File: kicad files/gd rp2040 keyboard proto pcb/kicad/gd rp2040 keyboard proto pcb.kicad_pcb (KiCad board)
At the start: 2 copper layers, 81.3 x 49.5 mm, 46 parts, among them J1 USB Pwr, J10 CTRL1-HDR, J11 CTRL2-HDR, J12 USB_A, J14 GPIO, J15 ADC, J2 Conn_01x02, J3 Power, J4 FTDI Header, J5 CTRL1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

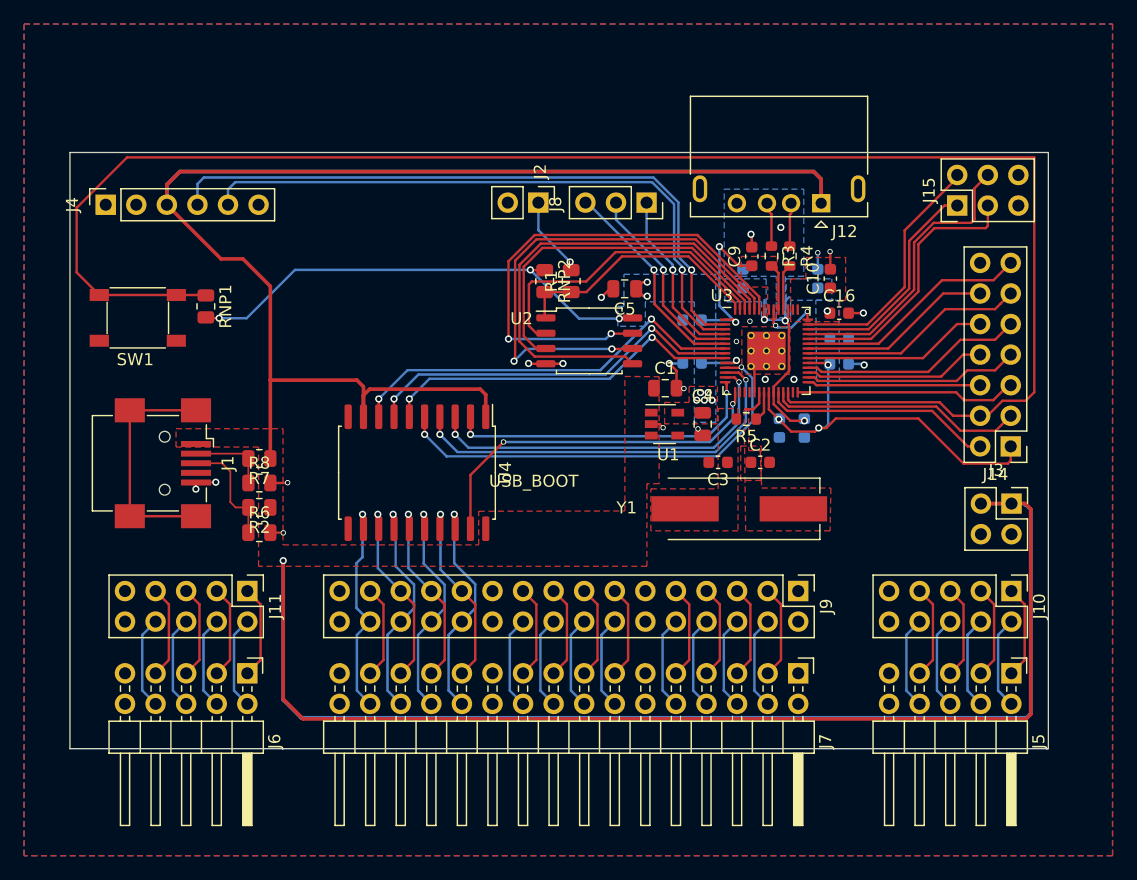
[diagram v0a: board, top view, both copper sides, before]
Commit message: schooched the left edge over to make mini-usb slightly hang over. added some GND vias through the board. re-routed some 3v3 signals for cleaner routes.
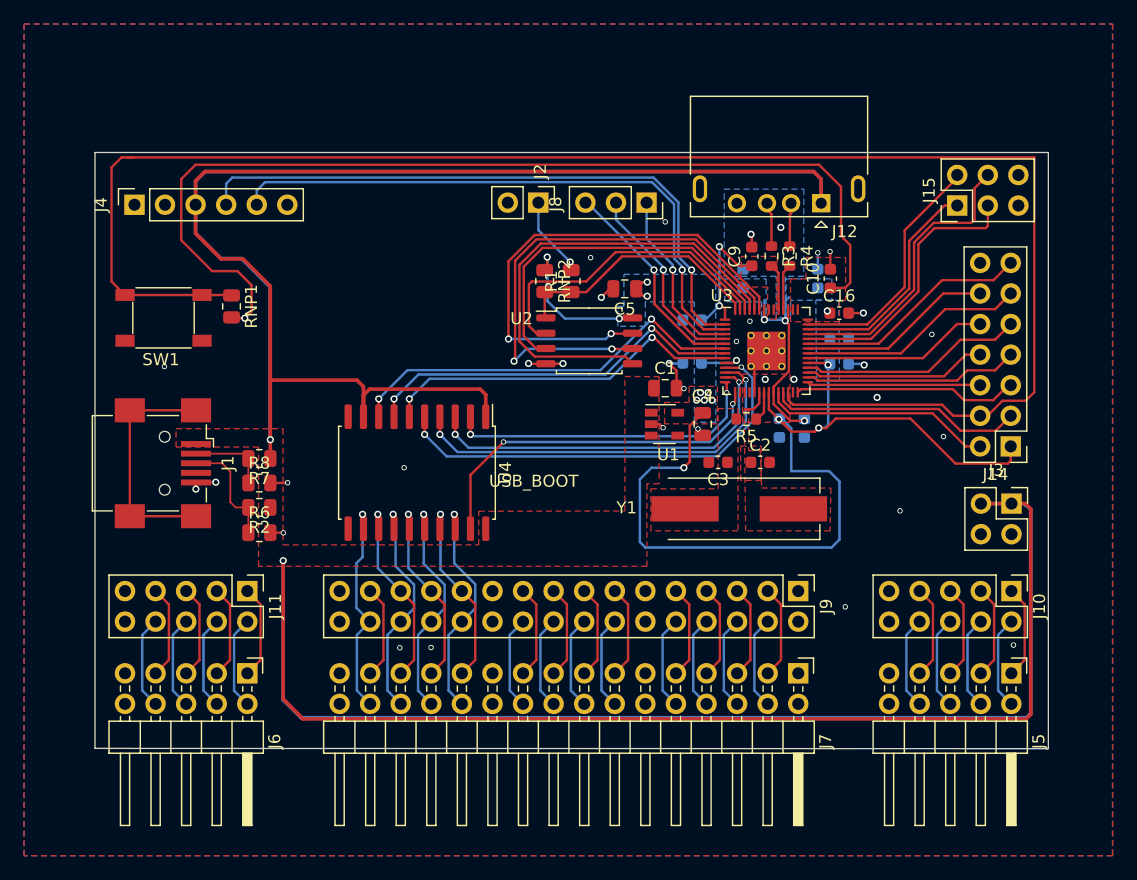
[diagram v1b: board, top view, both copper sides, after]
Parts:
- moved J4 2.39 mm to (67.6, 90.7)
- moved RNP1 2.13 mm to (75.7, 99.1)
- moved SW1 2.13 mm to (70.0, 100.1)
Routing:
- net +3V3: track 99.0 -> 192.0 mm, vias 19 -> 18
- net +5V: track 359.4 -> 377.1 mm, vias 1 -> 2
- net /TX_2040: track 52.6 -> 50.2 mm
- net /RX_2040: track 55.5 -> 53.1 mm
- net /RUN: track 140.1 -> 139.4 mm
- net GND: vias 21 -> 33
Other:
- board size 81.3 x 49.5 mm -> 79.2 x 49.5 mm

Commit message: silk clean up
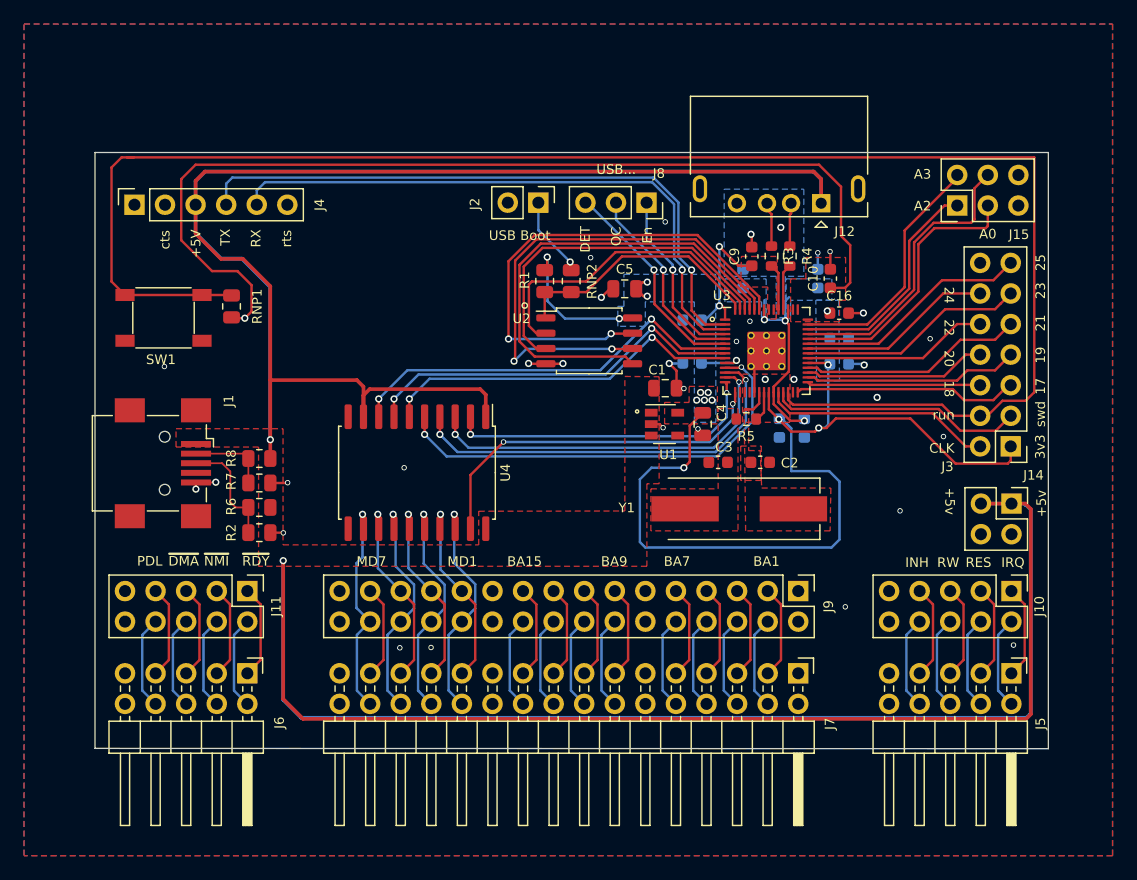
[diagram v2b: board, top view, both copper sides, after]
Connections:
- J1 pad 6: Net-(J1-Pad6) -> GND
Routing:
- net Net-(J1-Pad6): track 19.8 -> 0.00 mm
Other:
- board text added: "+5V"
- board text added: "+5v"
- board text added: "17"
- board text added: "18"
- board text added: "19"
- board text added: "20"
- board text added: "21"
- board text added: "22"
- board text added: "23"
- board text added: "24"
- board text added: "25"
- board text added: "3v3"
- board text added: "A0"
- board text added: "A2"
- board text added: "A3"
- board text added: "BA1"
- board text added: "BA15"
- board text added: "BA7"
- board text added: "BA9"
- board text added: "CLK"
- board text added: "D+"
- board text added: "D-"
- board text added: "DET"
- board text added: "En"
- board text added: "INH"
- board text added: "IRQ"
- board text added: "J10"
- board text added: "J11"
- board text added: "J2"
- board text added: "J5"
- board text added: "J6"
- board text added: "J7"
- board text added: "J8"
- board text added: "J9"
- board text added: "MD1"
- board text added: "MD7"
- board text added: "OC"
- board text added: "PDL"
- board text added: "RES"
- board text added: "RW"
- board text added: "RX"
- board text added: "TX"
- board text added: "USB Boot"
- board text added: "USB..."
- board text added: "cts"
- board text added: "rts"
- board text added: "run"
- board text added: "swd"
- board text added: "~DMA"
- board text added: "~NMI"
- board text added: "~RDY"
- board text removed: "USB_BOOT"

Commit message: rounded corners and added prototype area
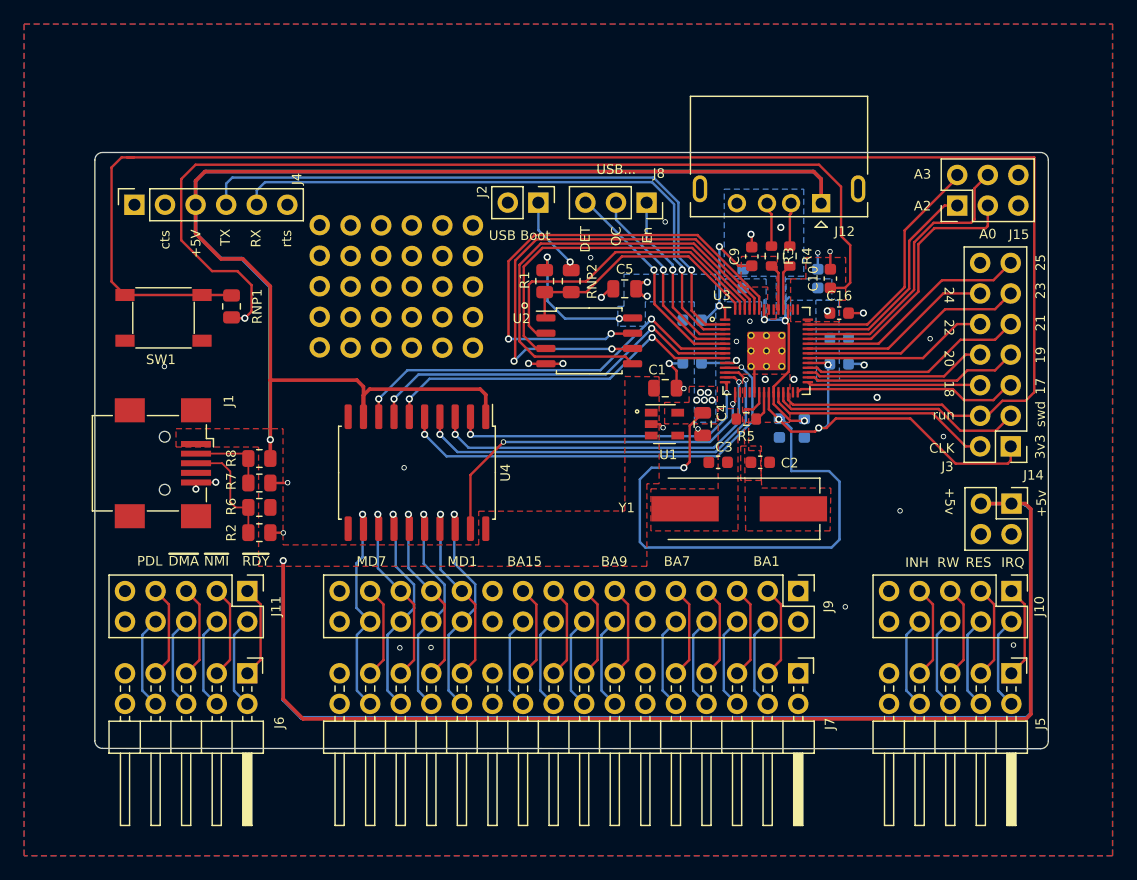
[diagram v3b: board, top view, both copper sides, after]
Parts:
- added J13: Conn_01x04, My Libraries:HoleField_1x05_P2.54mm, F.Cu at (83.0, 92.4)
- added J13: Conn_01x04, My Libraries:HoleField_1x05_P2.54mm, F.Cu at (85.5, 92.4)
- added J13: Conn_01x04, My Libraries:HoleField_1x05_P2.54mm, F.Cu at (88.1, 92.4)
- added J13: Conn_01x04, My Libraries:HoleField_1x05_P2.54mm, F.Cu at (90.6, 92.4)
- added J13: Conn_01x04, My Libraries:HoleField_1x05_P2.54mm, F.Cu at (93.2, 92.4)
- added J13: Conn_01x04, My Libraries:HoleField_1x05_P2.54mm, F.Cu at (95.7, 92.4)
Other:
- outline, holes or cut-outs redrawn

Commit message: adjusted ground pour around 5V USB in connector. considering moving buffer to make more prototyping room
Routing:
- net +5V: track 377.1 -> 380.0 mm
- net GND: track 25.6 -> 23.1 mm, vias 33 -> 36

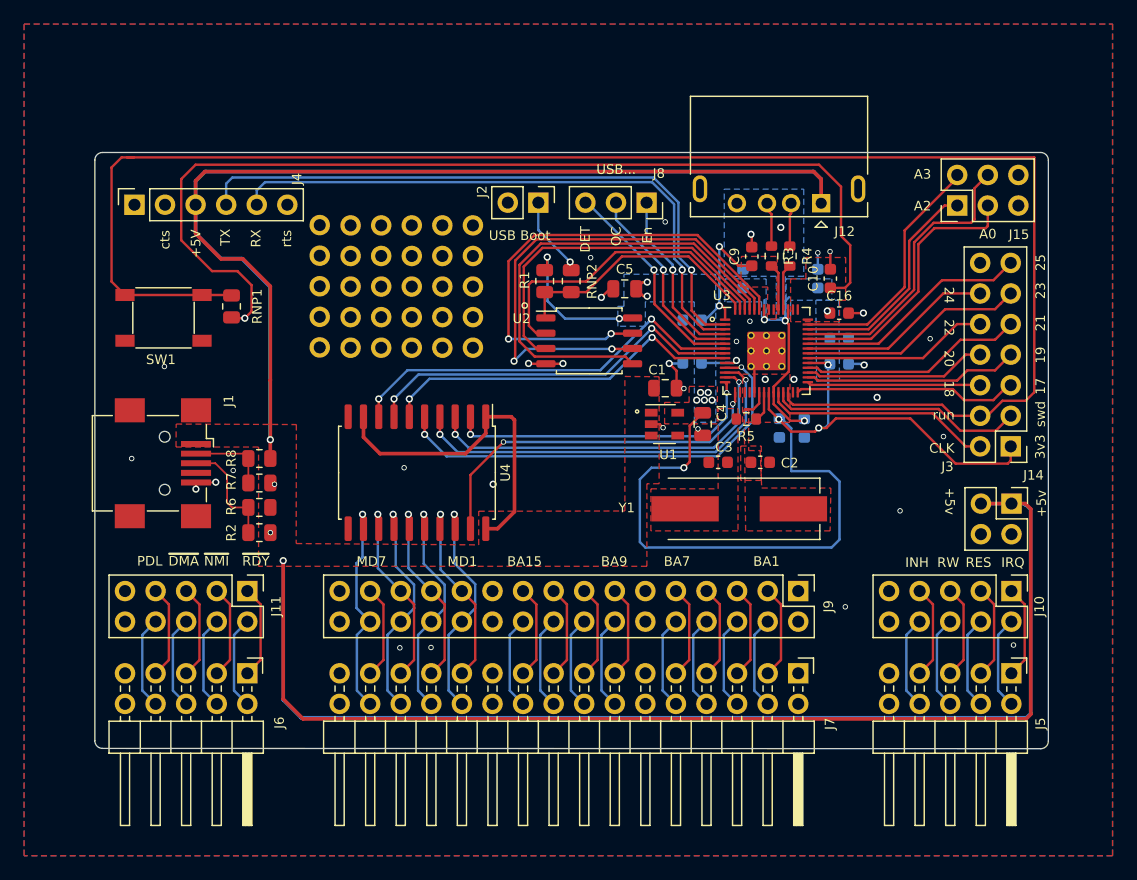
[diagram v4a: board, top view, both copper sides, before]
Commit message: added image and readme. added more prototyping holes after moving buffer
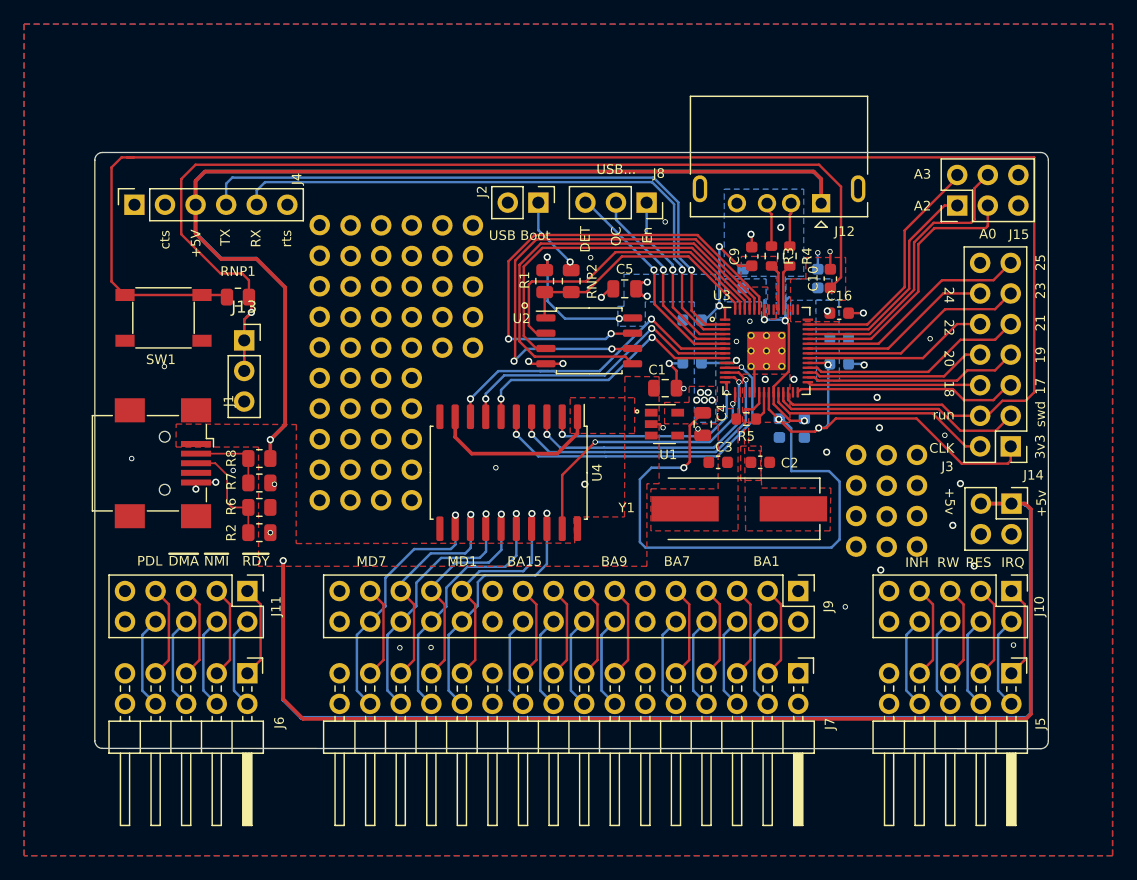
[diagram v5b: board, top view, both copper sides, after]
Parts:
- added J13: 3v3, Connector_PinSocket_2.54mm:PinSocket_1x03_P2.54mm_Vertical, F.Cu at (76.7, 102.0)
- added J13: Conn_01x04, My Libraries:HoleField_1x05_P2.54mm, F.Cu at (90.6, 105.1)
- added J13: Conn_01x04, My Libraries:HoleField_1x05_P2.54mm, F.Cu at (88.1, 105.1)
- added J13: Conn_01x04, My Libraries:HoleField_1x05_P2.54mm, F.Cu at (85.5, 105.1)
- added J13: Conn_01x04, My Libraries:HoleField_1x05_P2.54mm, F.Cu at (83.0, 105.1)
- added J8: Conn_01x04, My Libraries:HoleField_1x04_P2.54mm, F.Cu at (132.6, 111.5)
- added J8: Conn_01x04, My Libraries:HoleField_1x04_P2.54mm, F.Cu at (127.5, 111.5)
- added J8: Conn_01x04, My Libraries:HoleField_1x04_P2.54mm, F.Cu at (130.1, 111.5)
- moved U4 7.62 mm to (98.7, 113.0)
- moved RNP1 0.94 mm to (76.2, 98.4), turned to 0 degrees
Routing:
- net +5V: track 380.0 -> 370.3 mm
- net /245_EN: track 30.5 -> 22.9 mm
- net /D0: track 26.4 -> 18.8 mm
- net /D3: track 36.9 -> 29.3 mm
- net /D2: track 33.9 -> 26.3 mm
- net /D1: track 31.1 -> 23.5 mm
- net /D5: track 32.2 -> 24.8 mm
- net /D4: track 30.4 -> 23.2 mm
- net +3V3: track 192.0 -> 198.9 mm
- net /D6: track 33.9 -> 27.4 mm
- net /MD0: track 19.1 -> 23.4 mm
- net /MD1: track 16.7 -> 20.6 mm
- net /MD6: track 18.6 -> 22.5 mm
- net /MD2: track 19.1 -> 22.8 mm
- net /MD4: track 19.1 -> 22.7 mm
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
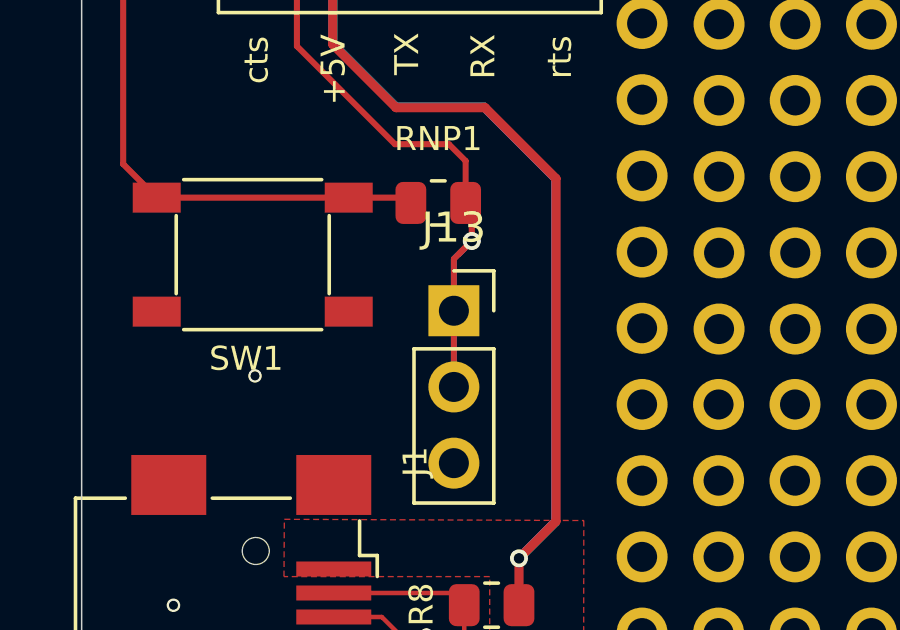
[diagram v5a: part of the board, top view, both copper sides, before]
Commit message: oh, now added prototyping holes.
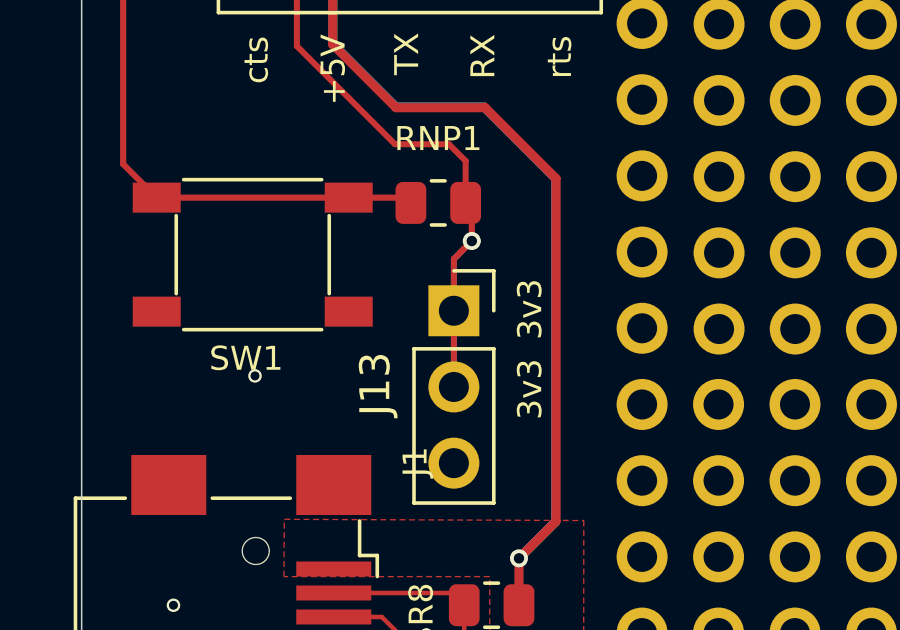
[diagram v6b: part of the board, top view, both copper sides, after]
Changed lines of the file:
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@@
   (general
     (thickness 1)
-    (drawings 105)
+    (drawings 109)
     (tracks 742)
     (zones 0)
@@
     (34 B.Paste user)
     (35 F.Paste user)
-    (36 B.SilkS user hide)
+    (36 B.SilkS user)
     (37 F.SilkS user)
     (38 B.Mask user)
@@
     (descr "Through hole straight socket strip, 1x03, 2.54mm pitch, single row (from Kicad 4.0.7), script generated")
     (tags "Through hole socket strip THT 1x03 2.54mm single row")
-    (fp_text reference J13 (at 0 -2.77) (layer F.SilkS)
+    (fp_text reference J13 (at -2.6162 2.4384 90) (layer F.SilkS)
       (effects (font (size 1 1) (thickness 0.15)))
     )
@@
     )
   )
+  (gr_text 3v3 (at 79.1591 101.8794 270) (layer B.SilkS)
+    (effects (font (size 0.8 0.8) (thickness 0.2)) (justify mirror))
+  )
+  (gr_text 3v3 (at 79.1464 104.5845 270) (layer B.SilkS)
+    (effects (font (size 0.8 0.8) (thickness 0.2)) (justify mirror))
+  )
+  (gr_text 3v3 (at 79.248 104.584485 90) (layer F.SilkS)
+    (effects (font (size 0.8 0.8) (thickness 0.2)))
+  )
+  (gr_text 3v3 (at 79.248 101.917485 90) (layer F.SilkS)
+    (effects (font (size 0.8 0.8) (thickness 0.2)))
+  )
   (gr_arc (start 142.875 86.995) (end 143.51 86.995) (angle -90) (layer Edge.Cuts) (width 0.05))

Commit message: final rp2040 pcb
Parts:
- added REF**: OSHW-Symbol_6.7x6mm_SilkScreen, Symbol:OSHW-Symbol_6.7x6mm_SilkScreen, B.Cu at (70.1, 103.9)
- added REF** (x2): KiCad-Logo2_5mm_Copper, Symbol:KiCad-Logo2_5mm_Copper, B.Cu at (118.0, 116.0)
- added svg2mod: G***, My Libraries:BE5v2, B.Cu at (132.8, 93.1)
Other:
- board text added: "gd rp2040/kbd 2021-09-06 r1 @baldengineer"
